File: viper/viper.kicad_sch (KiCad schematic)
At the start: 149 parts, among them Q1 2N7002, SW1 SW_Push, SW10 SW_Push, SW11 SW_Push, SW12 SW_Push, SW13 SW_Push, SW14 SW_Push, SW14_1 SW_Push, SW15 SW_Push, SW16 SW_Push, SW17 SW_Push, SW18 SW_Push, SW19 SW_Push, SW2 SW_Push, SW20 SW_Push, SW21 SW_Push, SW22 SW_Push, SW23 SW_Push, SW24 SW_Push, SW25 SW_Push, SW26 SW_Push, SW27 SW_Push, SW28 SW_Push, SW28_1 SW_Push, SW29 SW_Push, SW29_1 SW_Push, SW3 SW_Push, SW30 SW_Push, SW31 SW_Push, SW32 SW_Push, SW33 SW_Push, SW34 SW_Push, SW35 SW_Push, SW36 SW_Push, SW37 SW_Push, SW38 SW_Push, SW39 SW_Push, SW4 SW_Push, SW40 SW_Push, SW41 SW_Push, SW41_1 SW_Push, SW42 SW_Push, SW43 SW_Push, SW43_1 SW_Push, SW44 SW_Push, SW45 SW_Push, SW46 SW_Push, SW47 SW_Push, SW48 SW_Push, SW49 SW_Push, SW5 SW_Push, SW50 SW_Push, SW51 SW_Push, SW52 SW_Push, SW53 SW_Push, SW54 SW_Push, SW55 SW_Push, SW55_1 SW_Push, SW56 SW_Push, SW57 SW_Push, SW58 SW_Push, SW59 SW_Push, SW6 SW_Push, SW60 SW_Push, SW61 SW_Push, SW62 5.2x5.2mm, SW7 SW_Push, SW8 SW_Push, SW9 SW_Push, U1 ATmega32U4-MU, U2 PRTR5V0U2X, Y1 16Mhz

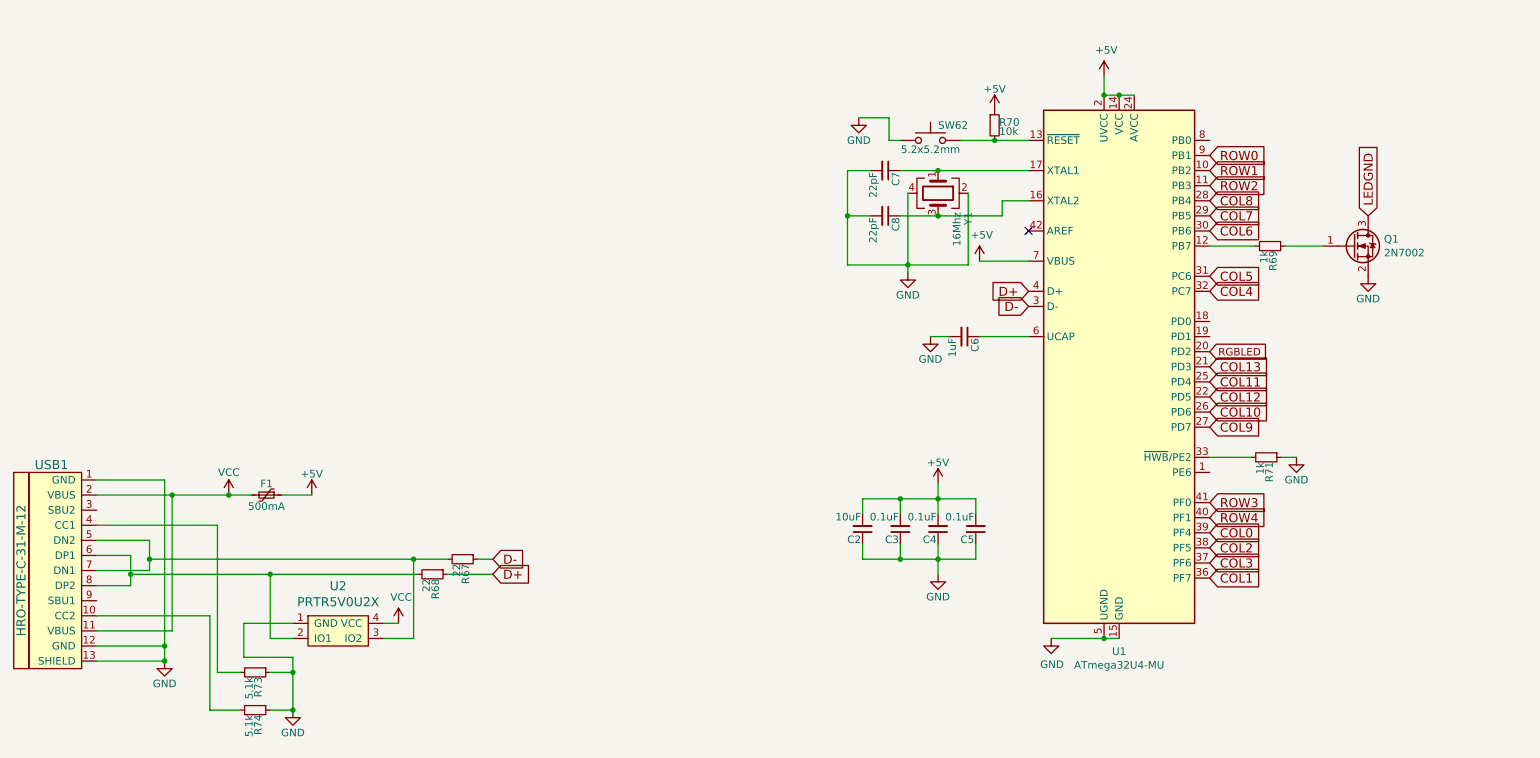
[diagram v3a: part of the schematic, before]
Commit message: MX Hybrid PCB, diode alignment is strange
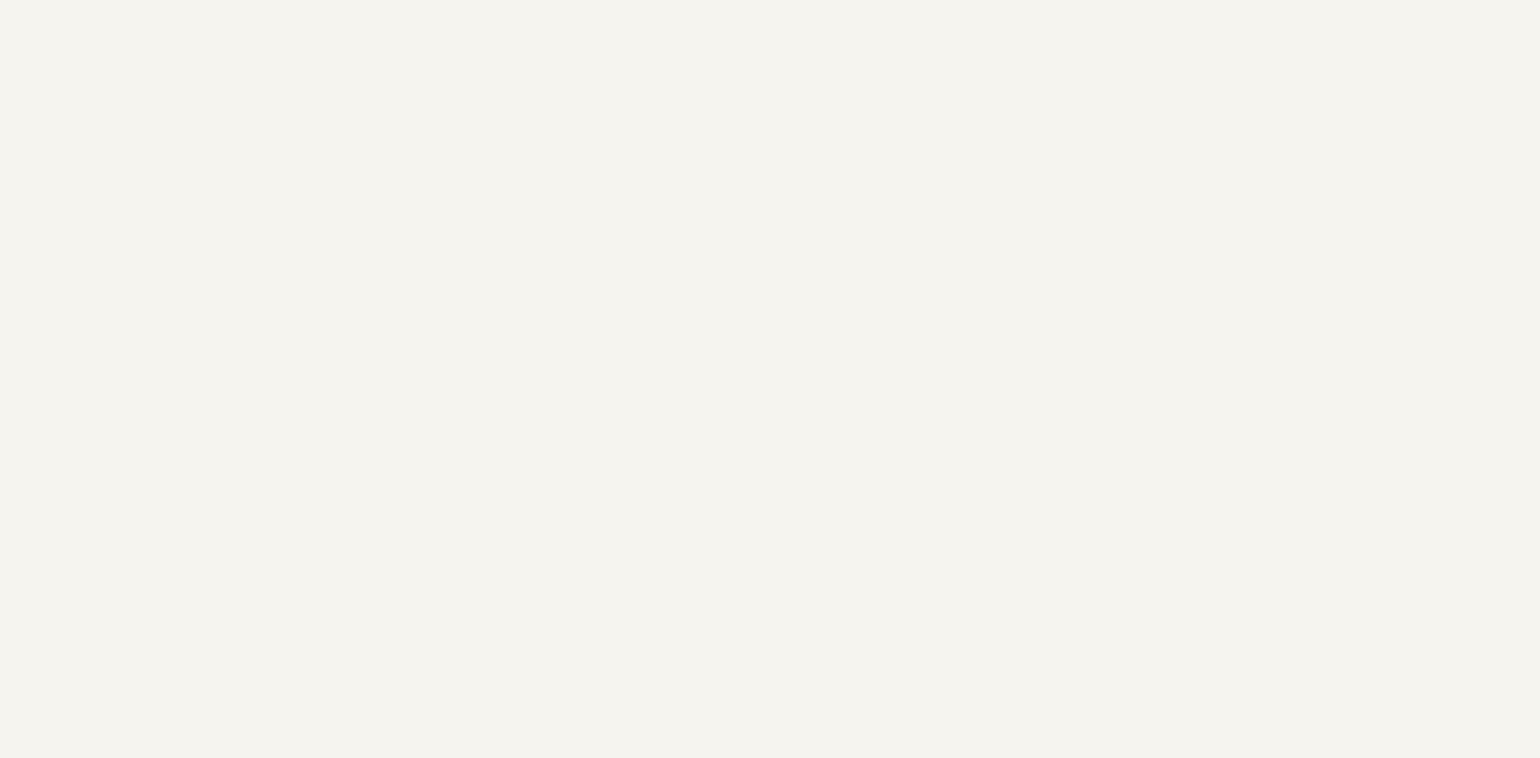
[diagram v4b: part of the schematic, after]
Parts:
- removed C2: 10uF, Capacitors_SMD:C_0603, symbol Device:C_Small
- removed C3, C4, C5: 0.1uF, Capacitors_SMD:C_0603, symbol Device:C_Small
- removed C6: 1uF, Capacitors_SMD:C_0603, symbol Device:C_Small
- removed C7, C8: 22pF, Capacitors_SMD:C_0603, symbol Device:C_Small
- removed F1: 500mA, Fuse_Holders_and_Fuses:Fuse_SMD1206_Reflow, symbol Device:Polyfuse_Small
- removed Q1: 2N7002, TO_SOT_Packages_SMD:SOT-23, symbol Transistor_FET:2N7002
- removed R67, R68: 22, Resistors_SMD:R_0805, symbol Device:R_Small
- removed R69, R71: 1k, Resistors_SMD:R_0805, symbol Device:R_Small
- removed R70: 10k, Resistors_SMD:R_0805, symbol Device:R_Small
- removed R73, R74: 5.1k, Resistors_SMD:R_0805, symbol Device:R_Small
- removed SW62: 5.2x5.2mm, Molex-0548190589:SKQG-1155865, symbol Voyager60-rescue:SW_Push
- removed U1: ATmega32U4-MU, Housings_DFN_QFN:QFN-44-1EP_7x7mm_Pitch0.5mm, symbol Voyager60-rescue:ATmega32U4-MU-MCU_Microchip_ATmega
- removed U2: PRTR5V0U2X, locallib:SOT143B, symbol ai03-locallib:PRTR5V0U2X
- removed USB1: HRO-TYPE-C-31-M-12, Type-C:HRO-TYPE-C-31-M-12-Assembly, symbol Type-C:HRO-TYPE-C-31-M-12
- removed Y1: 16Mhz, Crystals:Crystal_SMD_3225-4pin_3.2x2.5mm, symbol Device:Crystal_GND24
- SW1, SW10, SW11, SW12, SW13, SW14, SW14_1, SW15, SW16, SW17, SW18, SW19, SW2, SW20, SW21, SW22, SW23, SW24, SW25, SW26, SW27, SW28, SW28_1, SW29, SW29_1, SW3, SW30, SW31, SW32, SW33, SW34, SW35, SW36, SW37, SW38, SW39, SW4, SW40, SW41, SW41_1, SW42, SW43, SW43_1, SW44, SW45, SW46, SW47, SW48, SW49, SW5, SW50, SW51, SW52, SW53, SW54, SW55, SW55_1, SW56, SW57, SW58, SW59, SW6, SW60, SW61, SW7, SW8, SW9: footprint Switch_Keyboard_Cherry_MX:SW_Cherry_MX_PCB_1.00u -> Switch_Keyboard_Hybrid:SW_Hybrid_Cherry_MX_Alps_1.00u
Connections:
- no-connect marks 1 -> 0
